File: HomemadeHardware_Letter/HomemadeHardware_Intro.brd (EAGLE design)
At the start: 70 x 70 mm, 47 parts

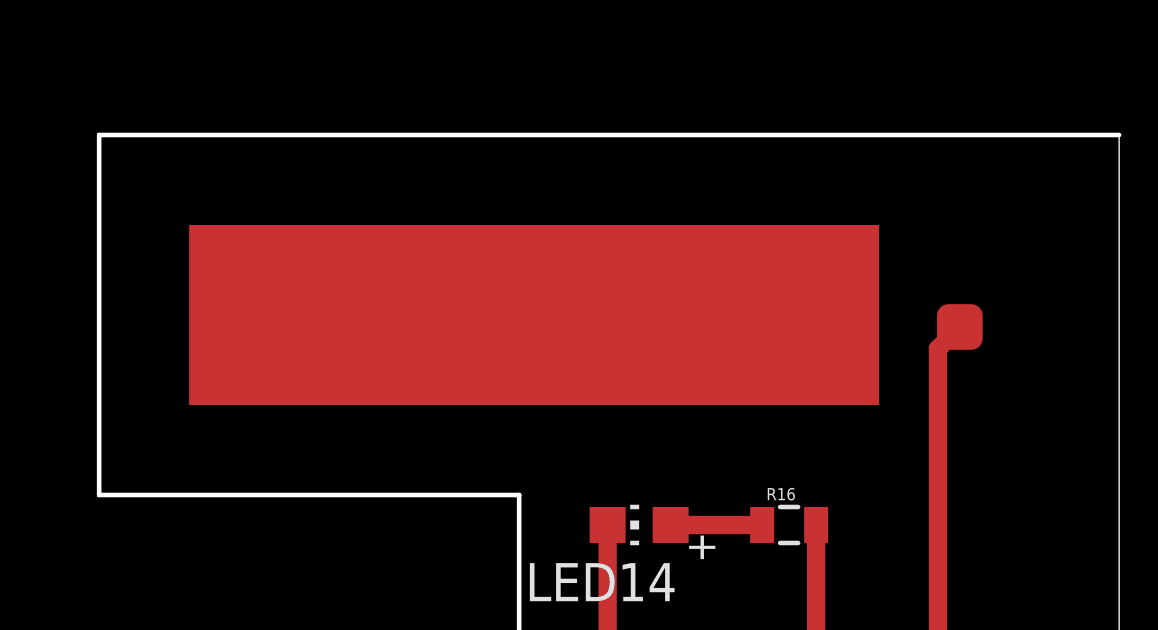
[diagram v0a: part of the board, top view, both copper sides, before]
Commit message: made on board capacitive sensor
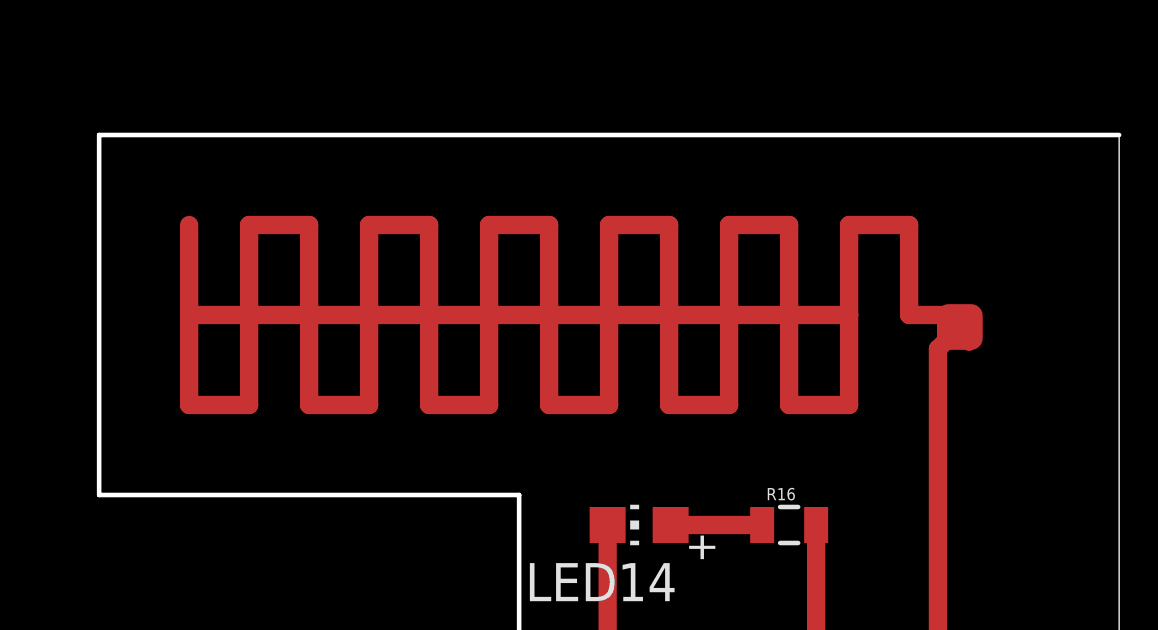
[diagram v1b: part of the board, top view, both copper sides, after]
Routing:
- net N$3: track 0.00 -> 124.0 mm
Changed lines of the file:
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@@
 <wire x1="36" y1="30" x2="36" y2="42" width="0.1524" layer="20"/>
 <wire x1="36" y1="42" x2="70" y2="42" width="0.1524" layer="20"/>
-<rectangle x1="39" y1="33" x2="62" y2="39" layer="1"/>
 </plain>
 <attributes>
@@
 <wire x1="63" y1="60.95" x2="54" y2="60.95" width="0" layer="19" extent="1-1"/>
 <wire x1="14.0500125" y1="34" x2="14" y2="34" width="0" layer="19" extent="1-1"/>
-<wire x1="14.0500125" y1="40" x2="14.0500125" y2="45" width="0" layer="19" extent="1-1"/>
+<wire x1="14.0500125" y1="45" x2="14.0500125" y2="40" width="0" layer="19" extent="1-1"/>
 <wire x1="34.5" y1="15.05000625" x2="41" y2="15.05" width="0" layer="19" extent="1-1"/>
 <wire x1="35" y1="60.95" x2="26" y2="60.95" width="0" layer="19" extent="1-1"/>
@@
 <wire x1="34.5" y1="11.4" x2="35" y2="10.9" width="0.6096" layer="1"/>
 </signal>
+<signal name="N$3">
+<wire x1="65" y1="36" x2="65" y2="35" width="0.4064" layer="1"/>
+<wire x1="39" y1="39" x2="39" y2="36" width="0.6096" layer="1"/>
+<wire x1="39" y1="36" x2="39" y2="33" width="0.6096" layer="1"/>
+<wire x1="39" y1="33" x2="41" y2="33" width="0.6096" layer="1"/>
+<wire x1="41" y1="33" x2="41" y2="39" width="0.6096" layer="1"/>
+<wire x1="41" y1="39" x2="43" y2="39" width="0.6096" layer="1"/>
+<wire x1="43" y1="39" x2="43" y2="33" width="0.6096" layer="1"/>
+<wire x1="43" y1="33" x2="45" y2="33" width="0.6096" layer="1"/>
+<wire x1="45" y1="33" x2="45" y2="39" width="0.6096" layer="1"/>
+<wire x1="45" y1="39" x2="47" y2="39" width="0.6096" layer="1"/>
+<wire x1="47" y1="39" x2="47" y2="33" width="0.6096" layer="1"/>
+<wire x1="47" y1="33" x2="49" y2="33" width="0.6096" layer="1"/>
+<wire x1="49" y1="33" x2="49" y2="39" width="0.6096" layer="1"/>
+<wire x1="49" y1="39" x2="51" y2="39" width="0.6096" layer="1"/>
+<wire x1="51" y1="39" x2="51" y2="33" width="0.6096" layer="1"/>
+<wire x1="51" y1="33" x2="53" y2="33" width="0.6096" layer="1"/>
+<wire x1="53" y1="33" x2="53" y2="39" width="0.6096" layer="1"/>
+<wire x1="53" y1="39" x2="55" y2="39" width="0.6096" layer="1"/>
+<wire x1="55" y1="39" x2="55" y2="33" width="0.6096" layer="1"/>
+<wire x1="55" y1="33" x2="57" y2="33" width="0.6096" layer="1"/>
+<wire x1="57" y1="33" x2="57" y2="39" width="0.6096" layer="1"/>
+<wire x1="57" y1="39" x2="59" y2="39" width="0.6096" layer="1"/>
+<wire x1="59" y1="39" x2="59" y2="33" width="0.6096" layer="1"/>
+<wire x1="59" y1="33" x2="61" y2="33" width="0.6096" layer="1"/>
+<wire x1="61" y1="33" x2="61" y2="36" width="0.6096" layer="1"/>
+<wire x1="61" y1="36" x2="61" y2="39" width="0.6096" layer="1"/>
+<wire x1="61" y1="39" x2="63" y2="39" width="0.6096" layer="1"/>
+<wire x1="63" y1="39" x2="63" y2="36" width="0.6096" layer="1"/>
+<wire x1="63" y1="36" x2="65" y2="36" width="0.6096" layer="1"/>
+<wire x1="39" y1="36" x2="61" y2="36" width="0.6096" layer="1"/>
+</signal>
 </signals>

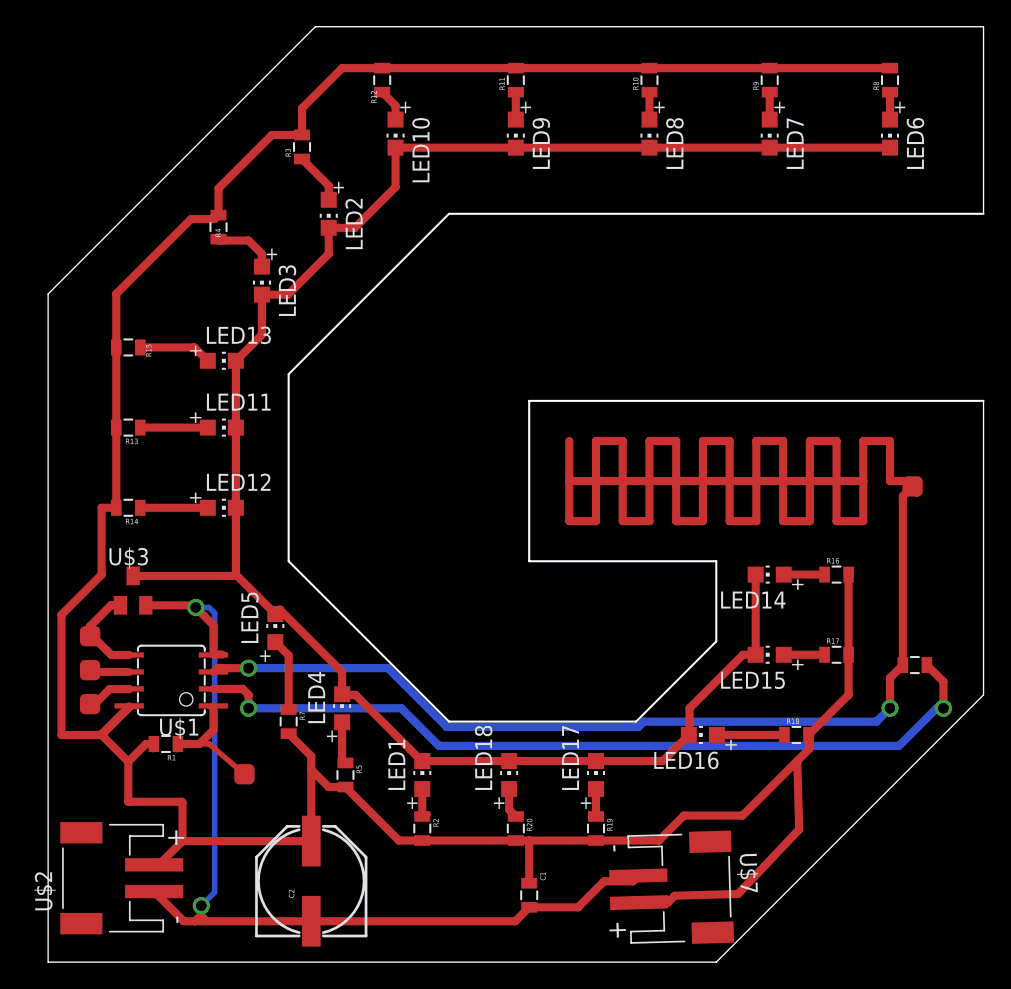
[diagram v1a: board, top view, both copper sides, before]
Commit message: fixed before pcb prunt. made some carves smaller
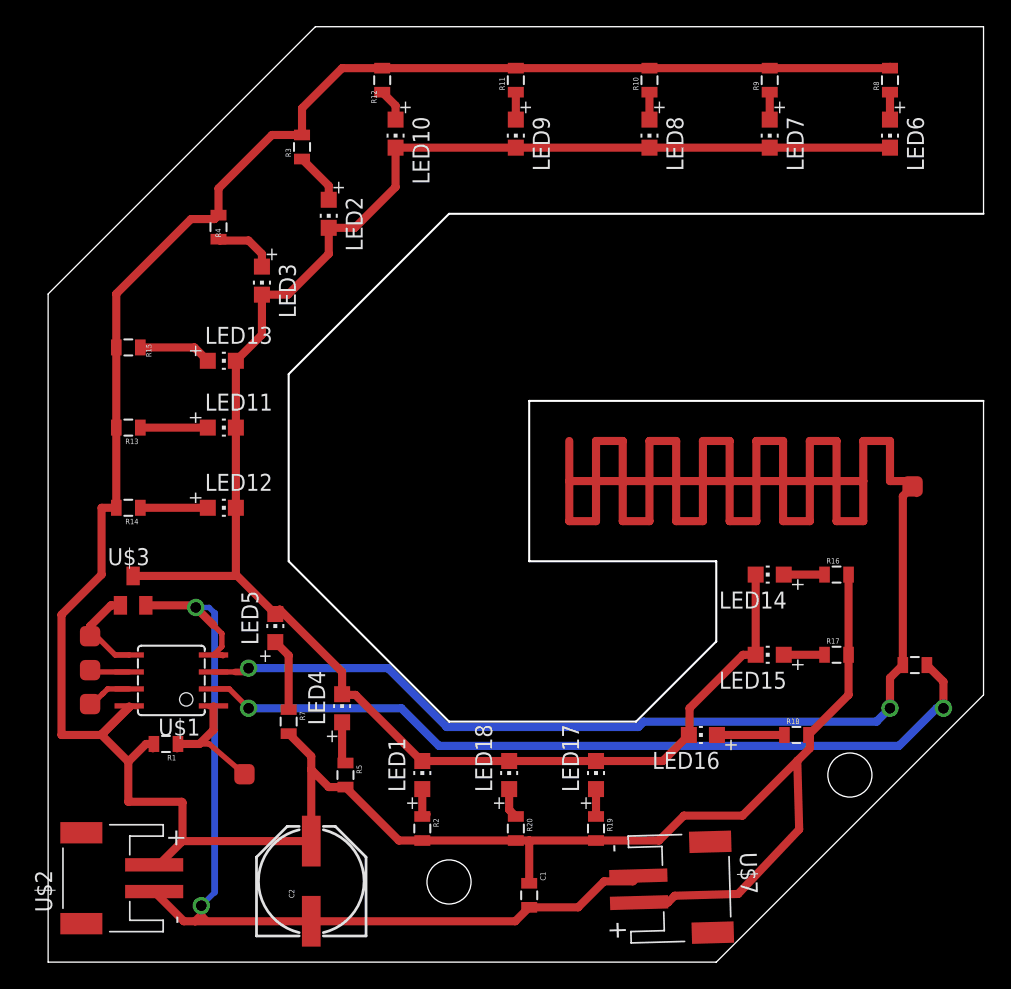
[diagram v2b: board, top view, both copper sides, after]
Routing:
- net N$12: track 11.9 -> 10.2 mm
- net N$11: track 62.1 -> 61.3 mm
